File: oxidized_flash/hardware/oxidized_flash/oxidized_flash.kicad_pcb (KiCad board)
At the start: 2 copper layers, 61 x 21.6 mm, 21 parts, among them J1 USB_A, J2 Conn_ARM_JTAG_SWD_10, U1 LM1117-3.3, U2 ATSAMD51G19A-MU, U3 MT25QL

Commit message: Remove 10k pullup on SWD_IO
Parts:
- removed R9: 10k, Resistors_SMD:R_0603
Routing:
- net /SWD_CLK: track 37.7 -> 32.7 mm
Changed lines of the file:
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@@
     (thickness 1.6)
     (drawings 6)
-    (tracks 369)
+    (tracks 366)
     (zones 0)
-    (modules 21)
+    (modules 20)
     (nets 57)
   )
@@
     )
   )
-  (module Resistors_SMD:R_0603 (layer F.Cu)
-    (at 66.548 36.83 180)
-    (descr "Resistor SMD 0603, reflow soldering, Vishay (see dcrcw.pdf)")
-    (tags "resistor 0603")
-    (attr smd)
-    (fp_text reference R9 (at 0 -1.45) (layer F.SilkS)
-      (effects (font (size 1 1) (thickness 0.15)))
-    )
-    (fp_text value 10k (at 0 1.5) (layer F.Fab)
-      (effects (font (size 1 1) (thickness 0.15)))
-    )
-    (fp_text user %R (at 0 0) (layer F.Fab)
-      (effects (font (size 0.4 0.4) (thickness 0.075)))
-    )
-    (fp_line (start -0.8 0.4) (end -0.8 -0.4) (layer F.Fab) (width 0.1))
-    (fp_line (start 0.8 0.4) (end -0.8 0.4) (layer F.Fab) (width 0.1))
-    (fp_line (start 0.8 -0.4) (end 0.8 0.4) (layer F.Fab) (width 0.1))
-    (fp_line (start -0.8 -0.4) (end 0.8 -0.4) (layer F.Fab) (width 0.1))
-    (fp_line (start 0.5 0.68) (end -0.5 0.68) (layer F.SilkS) (width 0.12))
-    (fp_line (start -0.5 -0.68) (end 0.5 -0.68) (layer F.SilkS) (width 0.12))
-    (fp_line (start -1.25 -0.7) (end 1.25 -0.7) (layer F.CrtYd) (width 0.05))
-    (fp_line (start -1.25 -0.7) (end -1.25 0.7) (layer F.CrtYd) (width 0.05))
-    (fp_line (start 1.25 0.7) (end 1.25 -0.7) (layer F.CrtYd) (width 0.05))
-    (fp_line (start 1.25 0.7) (end -1.25 0.7) (layer F.CrtYd) (width 0.05))
-    (pad 1 smd rect (at -0.75 0 180) (size 0.5 0.9) (layers F.Cu F.Paste F.Mask)
-      (net 3 +3V3))
-    (pad 2 smd rect (at 0.75 0 180) (size 0.5 0.9) (layers F.Cu F.Paste F.Mask)
-      (net 20 /SWD_CLK))
-    (model ${KISYS3DMOD}/Resistors_SMD.3dshapes/R_0603.wrl
-      (at (xyz 0 0 0))
-      (scale (xyz 1 1 1))
-      (rotate (xyz 0 0 0))
-    )
-  )
   (module Buttons_Switches_THT:SW_TH_Tactile_Omron_B3F-10xx (layer F.Cu)
     (at 75.692 28.448)
@@
   (segment (start 52.833 23.622) (end 52.808 23.622) (width 0.127) (layer F.Cu) (net 3))
   (segment (start 56.26425 27.72375) (end 56.26425 27.05325) (width 0.127) (layer F.Cu) (net 3))
-  (segment (start 55.421 37.338) (end 56.691 38.608) (width 0.25) (layer F.Cu) (net 3))
-  (segment (start 65.72 38.608) (end 67.298 37.03) (width 0.25) (layer F.Cu) (net 3))
-  (segment (start 67.298 37.03) (end 67.298 36.83) (width 0.25) (layer F.Cu) (net 3))
-  (segment (start 56.691 38.608) (end 65.72 38.608) (width 0.25) (layer F.Cu) (net 3))
-  (segment (start 71.546 34.148) (end 71.546 33.528) (width 0.25) (layer F.Cu) (net 3))
-  (segment (start 68.864 36.83) (end 71.546 34.148) (width 0.25) (layer F.Cu) (net 3))
-  (segment (start 67.298 36.83) (end 68.864 36.83) (width 0.25) (layer F.Cu) (net 3))
   (segment (start 72.376 33.528) (end 73.66 32.244) (width 0.25) (layer F.Cu) (net 3))
   (segment (start 71.546 33.528) (end 72.376 33.528) (width 0.25) (layer F.Cu) (net 3))
@@
   (segment (start 32.766 31.242) (end 33.016 31.242) (width 0.25) (layer F.Cu) (net 3))
   (segment (start 41.521001 37.965001) (end 54.743999 37.965001) (width 0.25) (layer F.Cu) (net 3))
+  (segment (start 56.691 38.608) (end 65.72 38.608) (width 0.25) (layer F.Cu) (net 3))
+  (segment (start 71.546 34.148) (end 71.546 33.528) (width 0.25) (layer F.Cu) (net 3))
+  (segment (start 65.72 38.608) (end 67.498 36.83) (width 0.25) (layer F.Cu) (net 3))
+  (segment (start 67.498 36.83) (end 68.864 36.83) (width 0.25) (layer F.Cu) (net 3))
+  (segment (start 55.421 37.338) (end 56.691 38.608) (width 0.25) (layer F.Cu) (net 3))
+  (segment (start 68.864 36.83) (end 71.546 34.148) (width 0.25) (layer F.Cu) (net 3))
   (segment (start 58.399001 24.031001) (end 57.76425 24.665752) (width 0.127) (layer F.Cu) (net 4))
   (segment (start 58.399001 23.529001) (end 58.399001 24.031001) (width 0.127) (layer F.Cu) (net 4))
@@
   (segment (start 53.997776 25.146) (end 55.76425 26.912474) (width 0.127) (layer F.Cu) (net 20))
   (segment (start 66.816 32.258) (end 67.646 32.258) (width 0.127) (layer F.Cu) (net 20))
-  (segment (start 65.798 33.276) (end 66.816 32.258) (width 0.127) (layer F.Cu) (net 20))
-  (segment (start 65.798 36.83) (end 65.798 33.276) (width 0.127) (layer F.Cu) (net 20))
   (segment (start 53.892562 25.40001) (end 55.26425 26.771698) (width 0.127) (layer F.Cu) (net 21))
   (segment (start 51.56201 25.40001) (end 53.892562 25.40001) (width 0.127) (layer F.Cu) (net 21))

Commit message: Add reset pin to SWD header
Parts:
- U2: value ATSAMD51G19A-MU -> ATSAMD51G18A-MU
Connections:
- U2 pad 40: Net-(U2-Pad40) -> /SWD_RST
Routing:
- net /SWD_RST: track 0.00 -> 11.2 mm, vias 0 -> 2
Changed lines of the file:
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@@
     (thickness 1.6)
     (drawings 6)
-    (tracks 366)
+    (tracks 375)
     (zones 0)
     (modules 20)
-    (nets 57)
+    (nets 56)
   )
   (page A4)
@@
   )
   (setup
-    (last_trace_width 0.25)
+    (last_trace_width 0.127)
     (user_trace_width 0.127)
     (trace_clearance 0.127)
@@
   (net 53 "Net-(U2-Pad1)")
   (net 54 "Net-(U2-Pad43)")
-  (net 55 "Net-(U2-Pad40)")
-  (net 56 "Net-(U3-Pad3)")
+  (net 55 "Net-(U3-Pad3)")
   (net_class Default "This is the default net class."
     (clearance 0.127)
@@
     (add_net "Net-(U2-Pad39)")
     (add_net "Net-(U2-Pad4)")
-    (add_net "Net-(U2-Pad40)")
     (add_net "Net-(U2-Pad43)")
     (add_net "Net-(U2-Pad47)")
@@
       (net 40 "Net-(U2-Pad16)"))
     (pad 3 smd rect (at -1.905 4.65 270) (size 0.5 1.8) (layers F.Cu F.Paste F.Mask)
-      (net 56 "Net-(U3-Pad3)"))
+      (net 55 "Net-(U3-Pad3)"))
     (pad 2 smd rect (at -3.175 4.65 270) (size 0.5 1.8) (layers F.Cu F.Paste F.Mask)
       (net 3 +3V3))
@@
     )
   )
+  (module Capacitors_SMD:C_0603 (layer F.Cu)
+    (at 44.462 24.13 180)
+    (descr "Capacitor SMD 0603, reflow soldering, AVX (see smccp.pdf)")
+    (tags "capacitor 0603")
+    (attr smd)
+    (fp_text reference C1 (at -0.242 1.524) (layer F.SilkS)
+      (effects (font (size 1 1) (thickness 0.15)))
+    )
+    (fp_text value 0.1u (at 0 1.5) (layer F.Fab)
+      (effects (font (size 1 1) (thickness 0.15)))
+    )
+    (fp_text user %R (at 0 0) (layer F.Fab)
+      (effects (font (size 0.3 0.3) (thickness 0.075)))
+    )
+    (fp_line (start -0.8 0.4) (end -0.8 -0.4) (layer F.Fab) (width 0.1))
+    (fp_line (start 0.8 0.4) (end -0.8 0.4) (layer F.Fab) (width 0.1))
+    (fp_line (start 0.8 -0.4) (end 0.8 0.4) (layer F.Fab) (width 0.1))
+    (fp_line (start -0.8 -0.4) (end 0.8 -0.4) (layer F.Fab) (width 0.1))
+    (fp_line (start -0.35 -0.6) (end 0.35 -0.6) (layer F.SilkS) (width 0.12))
+    (fp_line (start 0.35 0.6) (end -0.35 0.6) (layer F.SilkS) (width 0.12))
+    (fp_line (start -1.4 -0.65) (end 1.4 -0.65) (layer F.CrtYd) (width 0.05))
+    (fp_line (start -1.4 -0.65) (end -1.4 0.65) (layer F.CrtYd) (width 0.05))
+    (fp_line (start 1.4 0.65) (end 1.4 -0.65) (layer F.CrtYd) (width 0.05))
+    (fp_line (start 1.4 0.65) (end -1.4 0.65) (layer F.CrtYd) (width 0.05))
+    (pad 1 smd rect (at -0.75 0 180) (size 0.8 0.75) (layers F.Cu F.Paste F.Mask)
+      (net 3 +3V3))
+    (pad 2 smd rect (at 0.75 0 180) (size 0.8 0.75) (layers F.Cu F.Paste F.Mask)
+      (net 1 GND))
+    (model Capacitors_SMD.3dshapes/C_0603.wrl
+      (at (xyz 0 0 0))
+      (scale (xyz 1 1 1))
+      (rotate (xyz 0 0 0))
+    )
+  )
   (module Housings_DFN_QFN:QFN-48-1EP_7x7mm_Pitch0.5mm (layer F.Cu)
     (at 57.01425 31.12375)
@@
       (effects (font (size 1 1) (thickness 0.15)))
     )
-    (fp_text value ATSAMD51G19A-MU (at 0 4.75) (layer F.Fab)
+    (fp_text value ATSAMD51G18A-MU (at 0 4.75) (layer F.Fab)
       (effects (font (size 1 1) (thickness 0.15)))
     )
@@
       (net 4 "Net-(C6-Pad1)"))
     (pad 40 smd rect (at 1.25 -3.4 90) (size 0.7 0.25) (layers F.Cu F.Paste F.Mask)
-      (net 55 "Net-(U2-Pad40)"))
+      (net 2 /SWD_RST))
     (pad 39 smd rect (at 1.75 -3.4 90) (size 0.7 0.25) (layers F.Cu F.Paste F.Mask)
       (net 27 "Net-(U2-Pad39)"))
@@
       (net 53 "Net-(U2-Pad1)"))
     (model ${KISYS3DMOD}/Housings_DFN_QFN.3dshapes/QFN-48-1EP_7x7mm_Pitch0.5mm.wrl
-      (at (xyz 0 0 0))
-      (scale (xyz 1 1 1))
-      (rotate (xyz 0 0 0))
-    )
-  )
-  (module Capacitors_SMD:C_0603 (layer F.Cu)
-    (at 44.462 24.13 180)
-    (descr "Capacitor SMD 0603, reflow soldering, AVX (see smccp.pdf)")
-    (tags "capacitor 0603")
-    (attr smd)
-    (fp_text reference C1 (at -0.242 1.524) (layer F.SilkS)
-      (effects (font (size 1 1) (thickness 0.15)))
-    )
-    (fp_text value 0.1u (at 0 1.5) (layer F.Fab)
-      (effects (font (size 1 1) (thickness 0.15)))
-    )
-    (fp_text user %R (at 0 0) (layer F.Fab)
-      (effects (font (size 0.3 0.3) (thickness 0.075)))
-    )
-    (fp_line (start -0.8 0.4) (end -0.8 -0.4) (layer F.Fab) (width 0.1))
-    (fp_line (start 0.8 0.4) (end -0.8 0.4) (layer F.Fab) (width 0.1))
-    (fp_line (start 0.8 -0.4) (end 0.8 0.4) (layer F.Fab) (width 0.1))
-    (fp_line (start -0.8 -0.4) (end 0.8 -0.4) (layer F.Fab) (width 0.1))
-    (fp_line (start -0.35 -0.6) (end 0.35 -0.6) (layer F.SilkS) (width 0.12))
-    (fp_line (start 0.35 0.6) (end -0.35 0.6) (layer F.SilkS) (width 0.12))
-    (fp_line (start -1.4 -0.65) (end 1.4 -0.65) (layer F.CrtYd) (width 0.05))
-    (fp_line (start -1.4 -0.65) (end -1.4 0.65) (layer F.CrtYd) (width 0.05))
-    (fp_line (start 1.4 0.65) (end 1.4 -0.65) (layer F.CrtYd) (width 0.05))
-    (fp_line (start 1.4 0.65) (end -1.4 0.65) (layer F.CrtYd) (width 0.05))
-    (pad 1 smd rect (at -0.75 0 180) (size 0.8 0.75) (layers F.Cu F.Paste F.Mask)
-      (net 3 +3V3))
-    (pad 2 smd rect (at 0.75 0 180) (size 0.8 0.75) (layers F.Cu F.Paste F.Mask)
-      (net 1 GND))
-    (model Capacitors_SMD.3dshapes/C_0603.wrl
       (at (xyz 0 0 0))
       (scale (xyz 1 1 1))
@@
   (segment (start 77.102 25.576) (end 75.868 25.576) (width 0.127) (layer F.Cu) (net 1))
   (segment (start 75.868 25.576) (end 75.184 24.892) (width 0.127) (layer F.Cu) (net 1))
+  (segment (start 58.841 26.67) (end 58.928 26.67) (width 0.127) (layer F.Cu) (net 2))
+  (segment (start 58.26425 27.72375) (end 58.26425 27.24675) (width 0.127) (layer F.Cu) (net 2))
+  (via (at 58.928 26.67) (size 0.6) (drill 0.3) (layers F.Cu B.Cu) (net 2))
+  (segment (start 58.26425 27.24675) (end 58.841 26.67) (width 0.127) (layer F.Cu) (net 2))
+  (segment (start 58.928 26.67) (end 66.548 26.67) (width 0.127) (layer B.Cu) (net 2))
+  (via (at 67.056 27.178) (size 0.6) (drill 0.3) (layers F.Cu B.Cu) (net 2))
+  (segment (start 66.548 26.67) (end 67.056 27.178) (width 0.127) (layer B.Cu) (net 2))
+  (segment (start 67.646 27.768) (end 67.646 28.448) (width 0.127) (layer F.Cu) (net 2))
+  (segment (start 67.056 27.178) (end 67.646 27.768) (width 0.127) (layer F.Cu) (net 2))
   (segment (start 55.421 37.338) (end 55.396 37.338) (width 0.127) (layer F.Cu) (net 3))
   (segment (start 56.26425 36.49475) (end 55.421 37.338) (width 0.127) (layer F.Cu) (net 3))

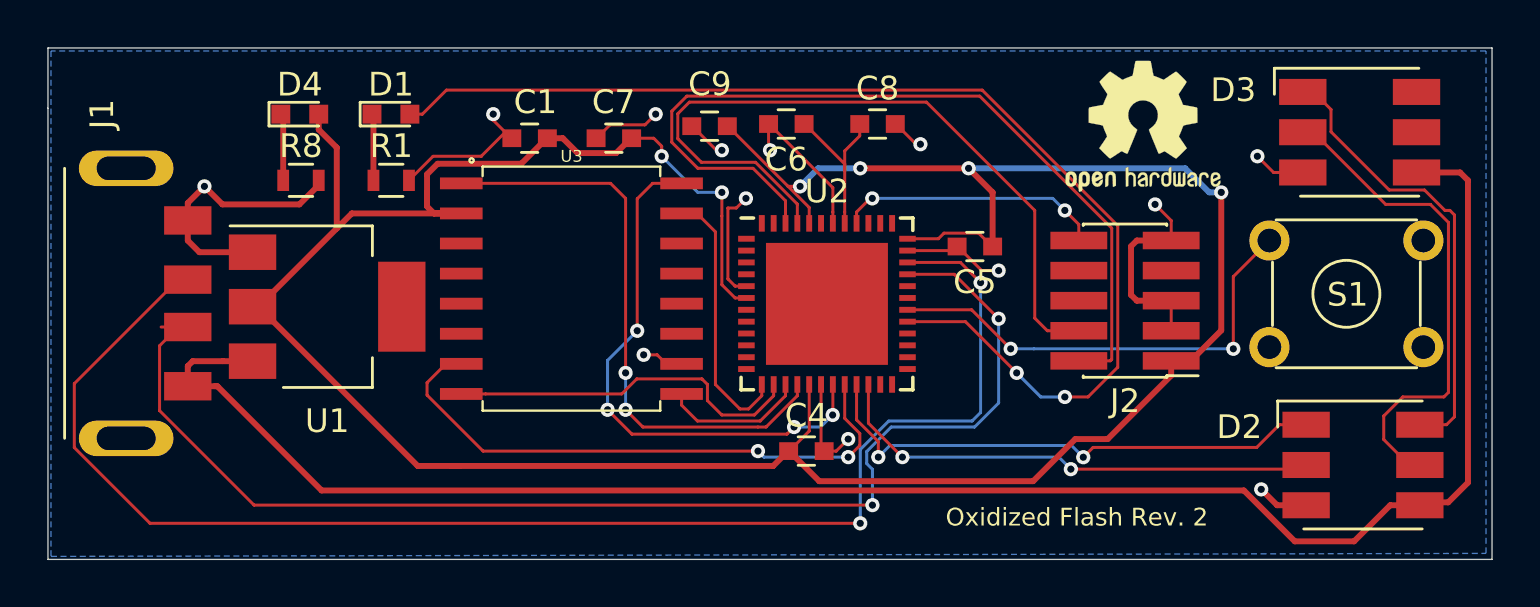
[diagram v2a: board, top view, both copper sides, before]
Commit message: Switch 0603 to handsoldering for more room
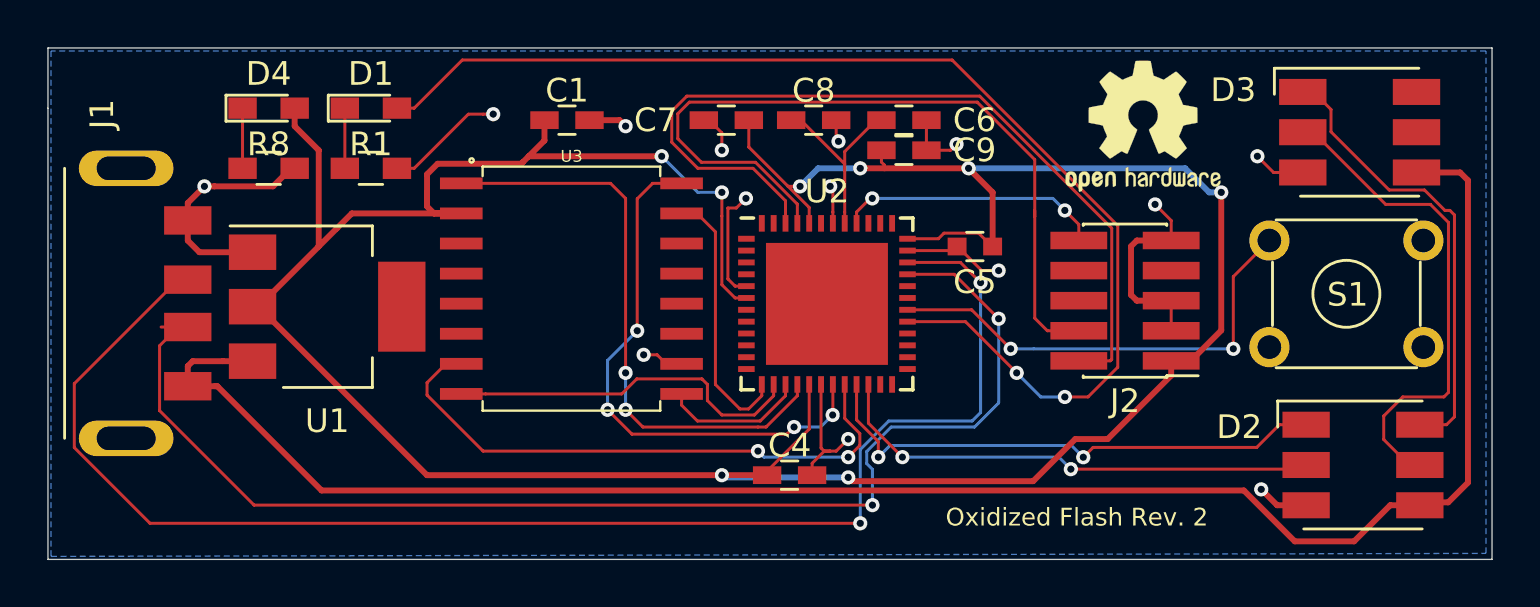
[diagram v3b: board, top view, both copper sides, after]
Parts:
- C1, C4, C6, C7, C8, C9: footprint Capacitors_SMD:C_0603 -> Capacitors_SMD:C_0603_HandSoldering
- D1, D4: footprint LEDs:LED_0603 -> LEDs:LED_0603_HandSoldering
- R1, R8: footprint Resistors_SMD:R_0603 -> Resistors_SMD:R_0603_HandSoldering
- moved C9 8.27 mm to (60.3, 24.6), turned to 0 degrees
- moved C6 4.97 mm to (60.3, 23.4), turned to 0 degrees
- moved C7 4.81 mm to (52.8, 23.4)
- moved C8 2.70 mm to (56.5, 23.4)
- moved C1 1.75 mm to (46.0, 23.4), turned to 0 degrees
- moved R8 1.46 mm to (33.4, 25.4)
- moved D4 1.34 mm to (33.4, 22.9)
- moved C4 1.24 mm to (55.4, 38.4)
- moved R1 1.00 mm to (37.8, 25.4)
- moved D1 0.88 mm to (37.8, 22.9)
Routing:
- net GND: track 58.9 -> 54.2 mm, vias 13 -> 14
- net +3V3: track 128.3 -> 132.9 mm, vias 6 -> 8
- net /SWD_CLK: track 32.7 -> 34.2 mm
- net /PA20: track 49.4 -> 50.9 mm
